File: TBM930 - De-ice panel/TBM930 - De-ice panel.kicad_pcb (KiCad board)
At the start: 2 copper layers, 190.5 x 101.6 mm, 91 parts, among them J1 SW_AIRFRAME_DE_ICE, J10 AVR-ISP-6, J11 Screw_Terminal_01x02, J2 SW_ICE_LIGHT, J3 SW_PROP_DE_ICE, J4 SW_WIND_SHIELD, J5 SW_PITOT_L_HTR, J6 SW_PITOT_R_HTR, J7 SW_INERT_SEP, J8 Barrel_Jack, J9 USB_B_Mini, SW1 SW_Push, SW2 SW_Push, U1 TLC5917IN, U2 TLC5917IN, U3 ATmega32U4-MU, Y1 Crystal_GND24

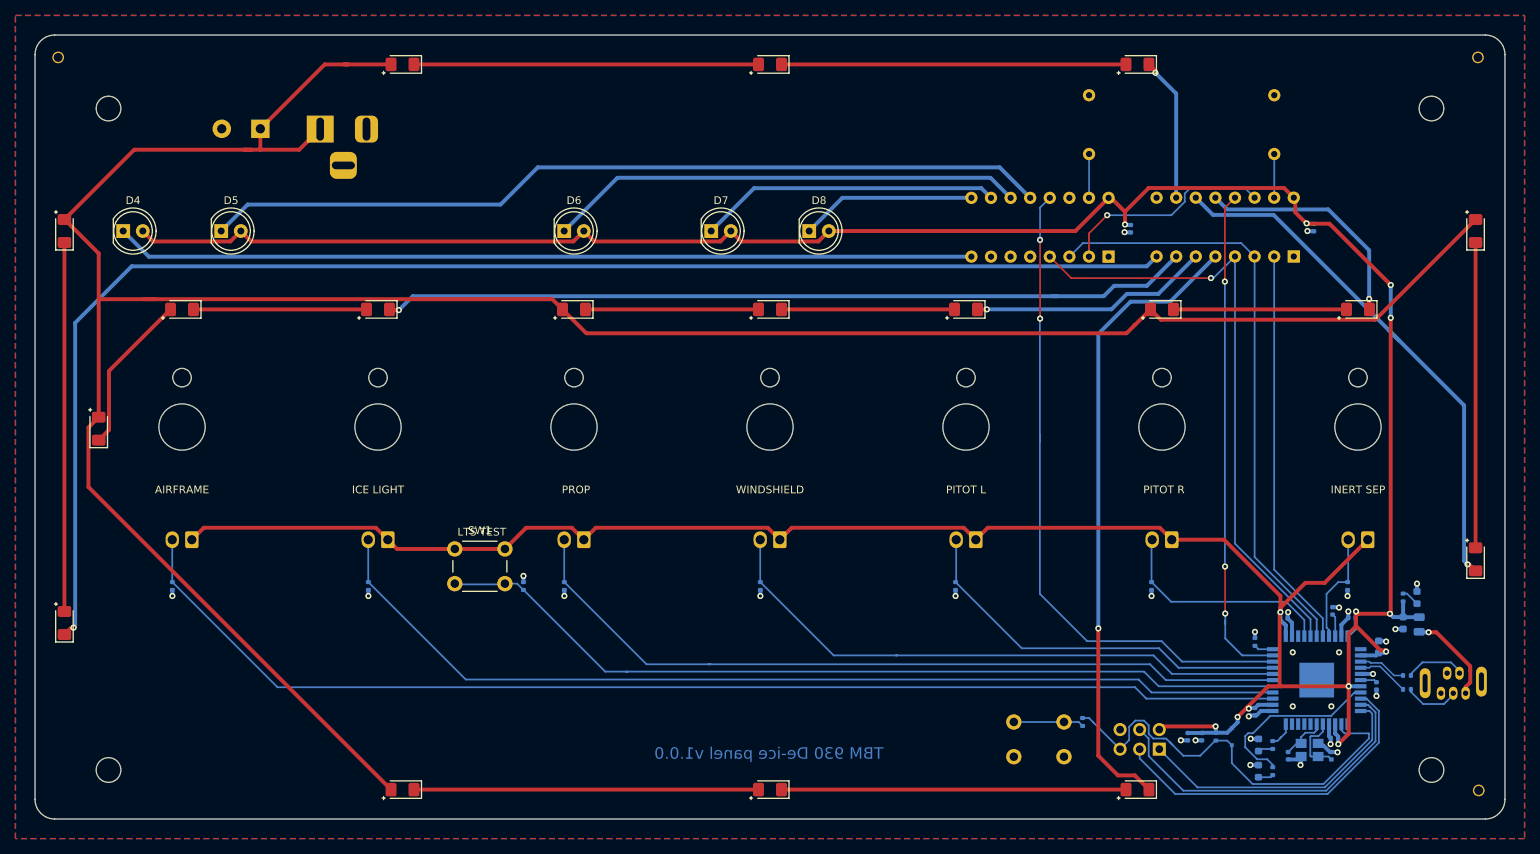
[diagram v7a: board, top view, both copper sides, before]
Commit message: Cleanup references so it should open on any machine
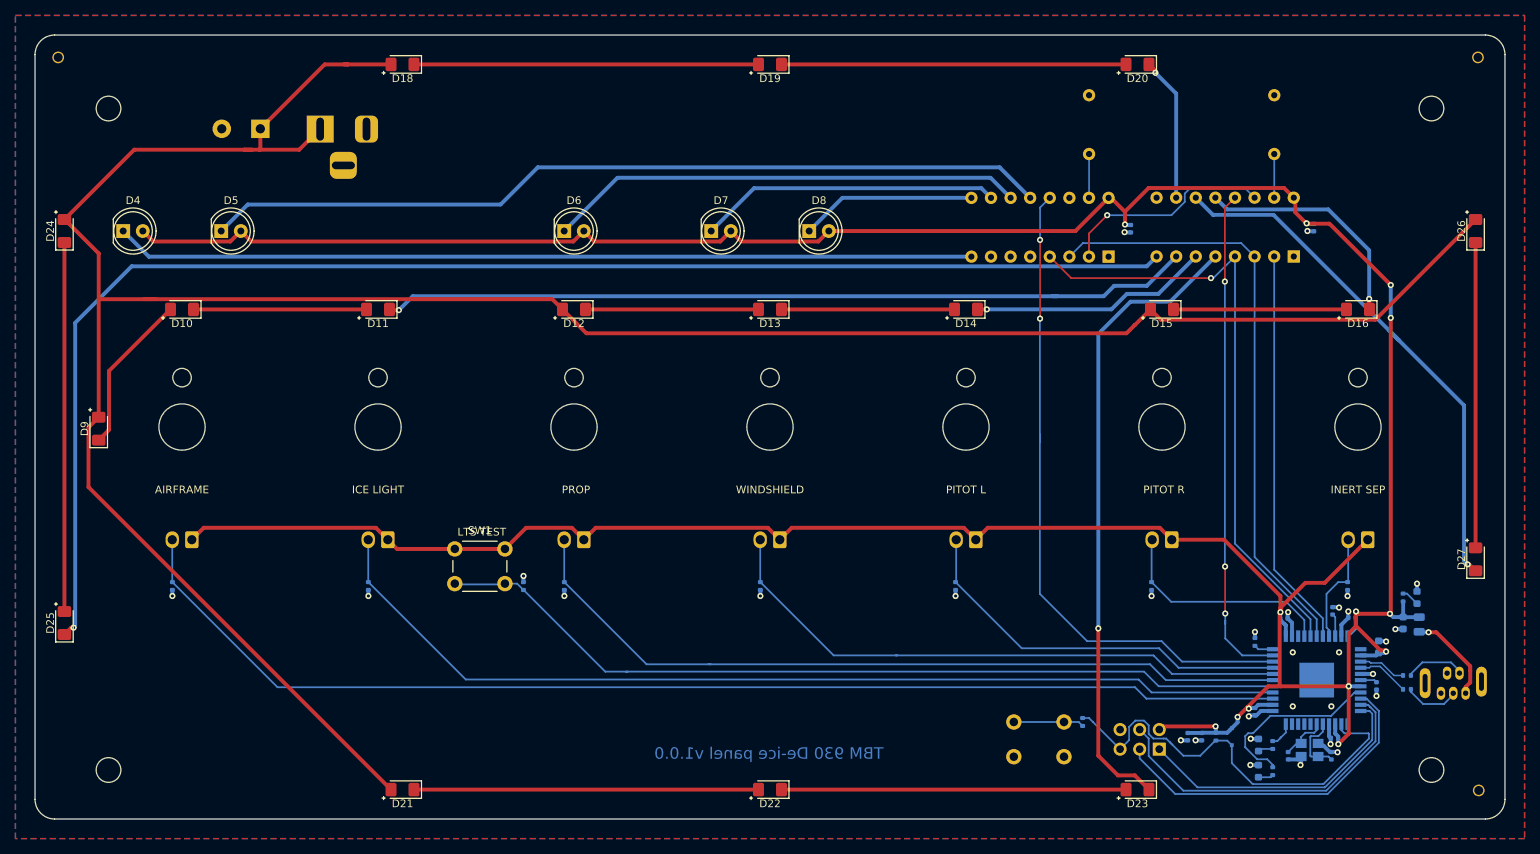
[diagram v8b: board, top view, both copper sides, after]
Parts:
- D1, D2, D3: footprint Global MobiFlight panel parts:LED_0603_1608Metric -> TBM930 - De-ice panel:LED_0603_1608Metric
- D10, D11, D12, D13, D14, D15, D16, D18, D19, D20, D21, D22, D23, D24, D25, D26, D27, D9: footprint Global MobiFlight panel parts:LED_1206_3216Metric_Pad1.42x1.75mm_HandSolder -> TBM930 - De-ice panel:LED_1206_3216Metric_Pad1.42x1.75mm_HandSolder
- J8: footprint Global MobiFlight panel parts:BarrelJack_Horizontal -> TBM930 - De-ice panel:BarrelJack_Horizontal
- J9: footprint Global MobiFlight panel parts:USB_B_Mini_Amphenol_UE25BE5510H -> TBM930 - De-ice panel:USB_B_Mini_Amphenol_UE25BE5510H
